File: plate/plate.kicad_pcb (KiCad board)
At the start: 2 copper layers, 145 x 56.2 mm, 18 parts, among them SW1 SW_Push, SW10 SW_Push, SW11 SW_Push, SW12 SW_Push, SW13 SW_Push, SW14 SW_Push, SW15 SW_Push, SW16 SW_Push, SW17 SW_Push, SW18 SW_Push, SW2 SW_Push, SW3 SW_Push, SW4 SW_Push, SW5 SW_Push, SW6 SW_Push, SW7 SW_Push, SW8 SW_Push, SW9 SW_Push

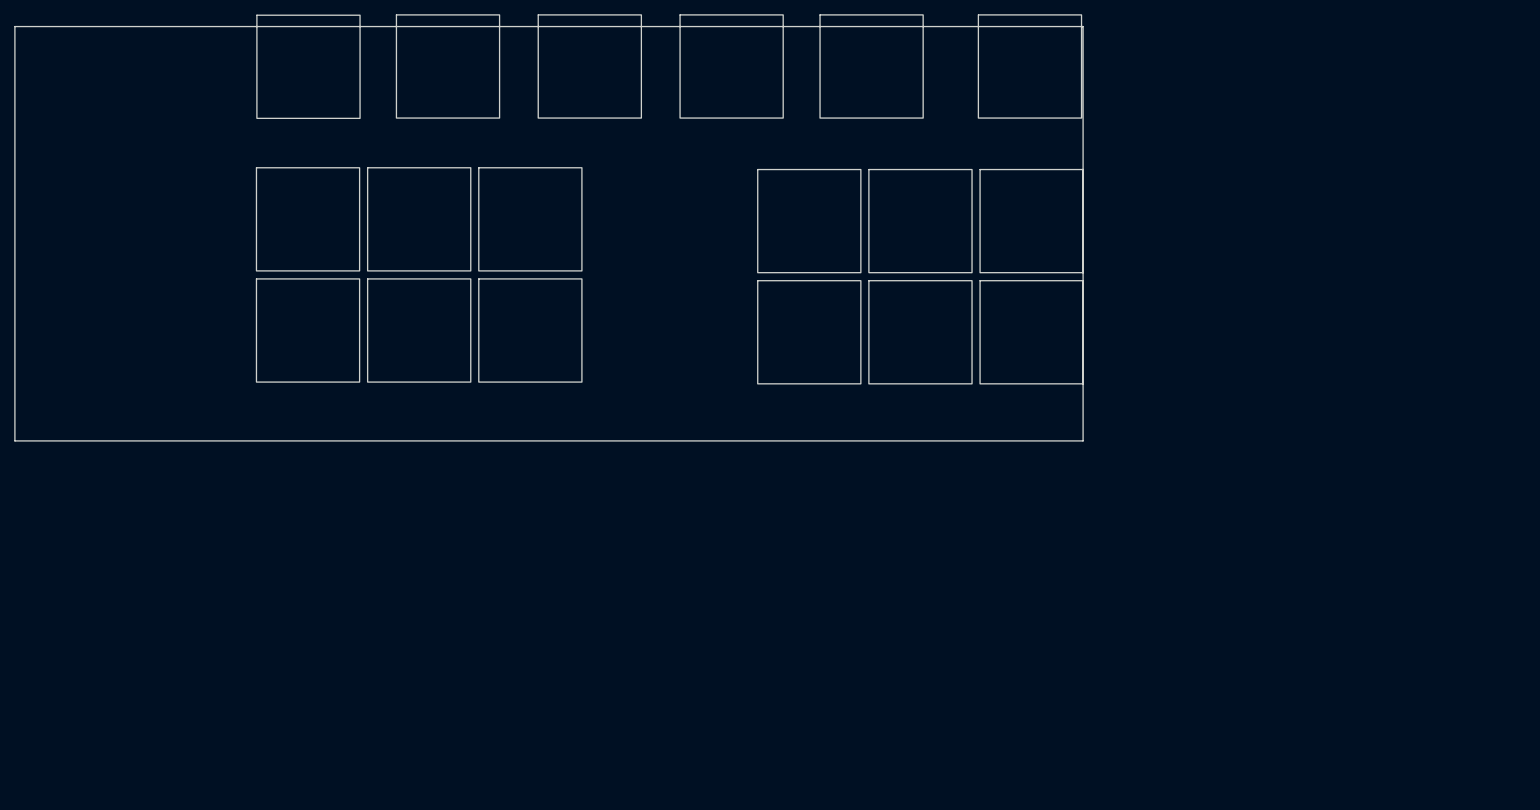
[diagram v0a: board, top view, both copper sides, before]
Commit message: Re-spaced all switches into a proper grid so it is properly manufacturable. I had to reroute, and I have updated the Gerbers and plate.stl files.
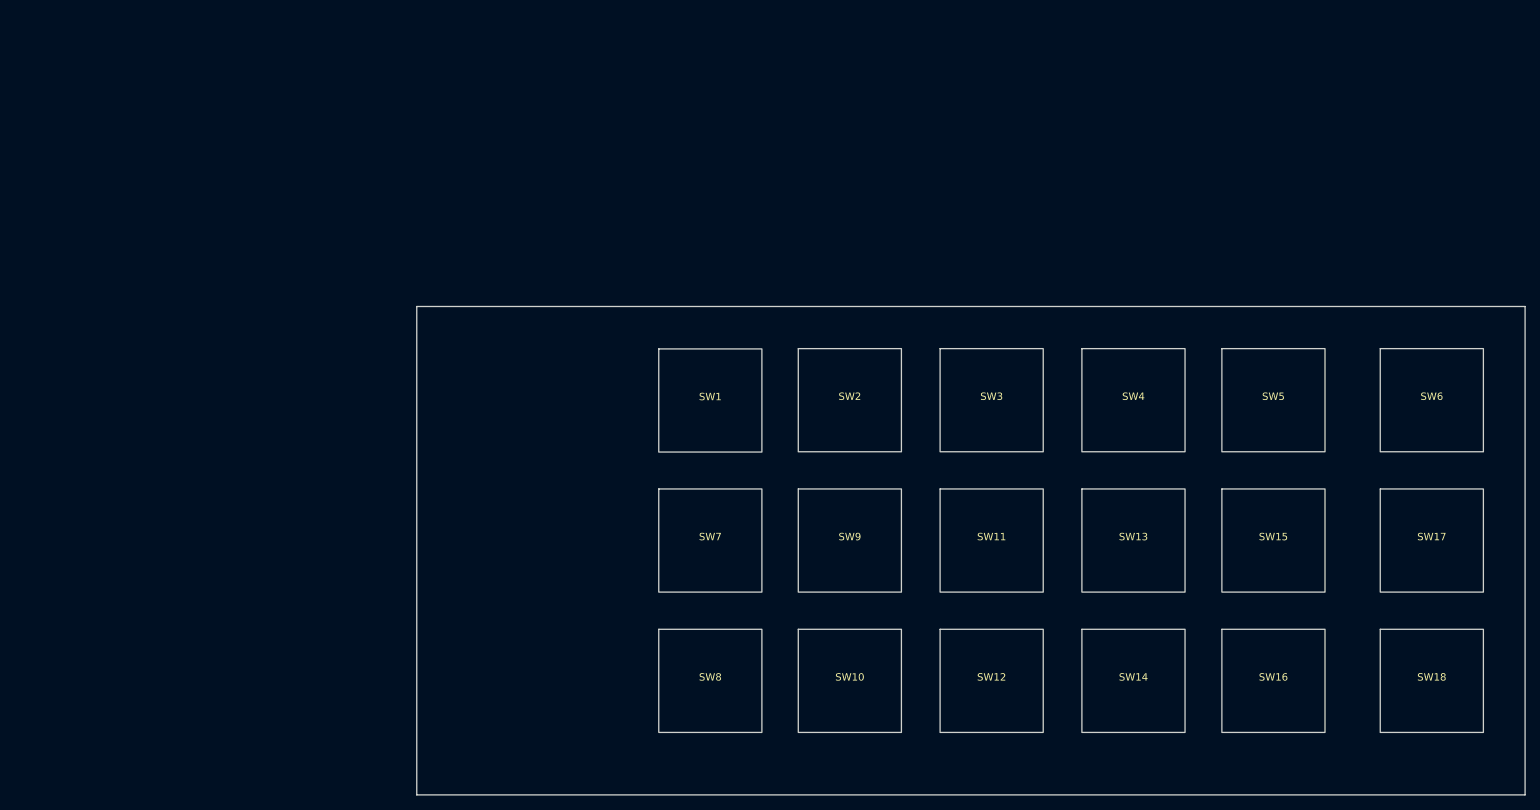
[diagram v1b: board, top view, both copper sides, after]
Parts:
- moved SW12 78.6 mm to (142.6, 98.8)
- moved SW11 76.3 mm to (142.6, 79.8)
- moved SW10 75.4 mm to (123.3, 98.8)
- moved SW9 72.9 mm to (123.3, 79.8)
- moved SW8 72.4 mm to (104.4, 98.8)
- moved SW18 72.0 mm to (202.3, 98.8)
- moved SW1 70.9 mm to (104.4, 60.8)
- moved SW2 70.9 mm to (123.3, 60.7)
- moved SW3 70.9 mm to (142.6, 60.7)
- moved SW4 70.9 mm to (161.8, 60.7)
- moved SW5 70.9 mm to (180.8, 60.7)
- moved SW6 70.9 mm to (202.3, 60.7)
- moved SW7 69.9 mm to (104.4, 79.8)
- moved SW17 69.5 mm to (202.3, 79.8)
- moved SW16 67.3 mm to (180.8, 98.8)
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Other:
- board size 145 x 56.2 mm -> 150.4 x 66.3 mm
